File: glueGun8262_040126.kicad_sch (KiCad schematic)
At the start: 35 parts, among them CN1 KF243-5.0-2P, CN2 KF243-5.0-2P, CN3 KF243-5.0-2P, CN4 KF243-5.0-2P, CN5 KF243-5.0-2P, CN6 KF243-5.0-2P, U1 DRV8262DDWR, U2 DRV8262DDWR, U3 ESP32-S3-DEVKITC-1-N8R2, U4 INA4181A1IPWR

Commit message: ina240 schunts in series with sol
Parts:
- removed C11, C12, C13, C14: 10nf 100v, Capacitor_SMD:C_0603_1608Metric, symbol Device:C
- removed C15: 100nf 10v, Capacitor_SMD:C_0402_1005Metric, symbol Device:C
- removed R10, R7, R8, R9: 50mh, Resistor_SMD:R_1206_3216Metric, symbol Device:R
- removed U4: INA4181A1IPWR, easyeda2kicad:TSSOP-20_L6.5-W4.4-P0.65-LS6.4-BL, symbol easyeda2kicad:INA4181A1IPWR
- added C16: 10uf 50v, Capacitor_SMD:C_1206_3216Metric, symbol Device:C
- added C17: 22uf 10v, Capacitor_SMD:C_1206_3216Metric, symbol Device:C
- added C18, C19, C20, C21: 100nf, Capacitor_SMD:C_0603_1608Metric, symbol Device:C
- added CN7: KF243-5.0-2P, easyeda2kicad:CONN-TH_P5.00_KF243-5.0-2P, symbol easyeda2kicad:KF243-5.0-2P
- added CN9: KF243-5.0-4P, easyeda2kicad:CONN-TH_4P-P5.00_KF243-5.0-4P, symbol easyeda2kicad:KF243-5.0-4P
- added D1: D_Schottky, Package_TO_SOT_SMD:SOT-23, symbol Device:D_Schottky
- added D2, D3, D4, D5: green, LED_SMD:LED_0805_2012Metric, symbol Device:LED
- added NT1, NT3, NT4, NT5, NT6, NT7, NT8: NetTie_2, NetTie-2_SMD_Pad0.5mm, symbol Device:NetTie_2
- added NT2: NetTie_2, NetTie:NetTie-2_SMD_Pad0.5mm, symbol Device:NetTie_2
- added R11: 470r, Resistor_SMD:R_0201_0603Metric, symbol Device:R
- added R12, R13, R15, R16: 2.2k, Resistor_SMD:R_1206_3216Metric, symbol Device:R
- added R14: 5.1k, Resistor_SMD:R_0402_1005Metric, symbol Device:R
- added R17, R18, R19, R20: 40m, Resistor_SMD:R_2512_6332Metric, symbol Device:R
- added RN2: 10k, Resistor_SMD:R_Array_Convex_4x0603, symbol Device:R_Pack04
- added U10, U11, U6, U7: INA240A2DR, easyeda2kicad:SOIC-8_L4.9-W3.9-P1.27-LS6.0-BL, symbol easyeda2kicad:INA240A2DR
- added U5: 6N137, Package_DIP:DIP-8_W7.62mm, symbol Isolator:6N137
- added U8: K7805-1000R3_C2992391, easyeda2kicad:PWRM-TH_YLPTEC_K78XX-1000R3, symbol easyeda2kicad:K7805-1000R3_C2992391
- added U9: TLP281-4(GB-TP,J,F, easyeda2kicad:SOP-16_L10.3-W4.4-P1.27-LS7.0-BL, symbol easyeda2kicad:TLP281-4(GB-TP,J,F
- R1, R2, R3, R4, R5, R6: footprint Resistor_SMD:R_0805_2012Metric -> Resistor_SMD:R_0201_0603Metric
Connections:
- net U1_PGND12 is gone; now on net GND: U1.10 (PGND), U1.3 (PGND)
- net U1_PGND34 is gone; now on net GND: U1.13 (PGND), U1.20 (PGND)
- net U2_PGND12 is gone; now on net GND: U2.10 (PGND), U2.3 (PGND)
- net U2_PGND34 is gone; now on net GND: U2.13 (PGND), U2.20 (PGND)
- net +3V3: now also C18.1, C19.1, C20.1, C21.1, R14.1, RN2.5 (R4.2), RN2.6 (R3.2), RN2.7 (R2.2), RN2.8 (R1.2), U10.6 (VS), U11.6 (VS), U6.6 (VS), U7.6 (VS)
- net GND: now also CN6.2, C16.2, C17.2, C18.2, C19.2, C20.2, C21.2, U10.2 (GND), U10.3 (REF2), U10.7 (REF1), U11.2 (GND), U11.3 (REF2), U11.7 (REF1), U5.5 (GND), U6.2 (GND), U6.3 (REF2), U6.7 (REF1), U7.2 (GND), U7.3 (REF2), U7.7 (REF1), U8.2 (GND), U9.11 (EM), U9.13 (EM), U9.15 (EM), U9.2 (CAT), U9.4 (CAT), U9.6 (CAT), U9.8 (CAT), U9.9 (EM)
- net Gun1Vref: now also U6.5 (OUT)
- net Gun2Vref: now also U7.5 (OUT)
- net Gun3Vref: now also U10.5 (OUT)
- net Gun4Vref: now also U11.5 (OUT)
- net U2_OUT1: now reaches U2.4 (OUT1), U2.5 (OUT1), U2.6 (OUT1)
- net U2_OUT1: now also NT7.2, R19.2; no longer CN4.1
- net U2_OUT2: now reaches CN4.2, U2.7 (OUT2), U2.8 (OUT2), U2.9 (OUT2)
- net +5V: now reaches U3.J1_21 (5V0)
- net +5V: now also C17.1, U5.7 (EN), U5.8 (VCC), U8.3 (+VO)
- net Input_1_24v: now reaches U3.J3_10 (GPIO38)
- net Input_1_24v: now also RN2.1 (R1.1), U9.16 (COL)
- net Input_4_24v: now reaches U3.J3_16 (GPIO48)
- net Input_4_24v: now also RN2.4 (R4.1), U9.10 (COL)
- net Input_3_24v: now reaches U3.J3_17 (GPIO47)
- net Input_3_24v: now also RN2.3 (R3.1), U9.12 (COL)
- net Input_0_5v: now reaches U3.J3_18 (GPIO21)
- net Input_0_5v: now also R14.2, U5.6 (VO)
- net Input_2_24v: now reaches U3.J3_9 (MTCK/GPIO39)
- net Input_2_24v: now also RN2.2 (R2.1), U9.14 (COL)
- net U1_OUT3: now reaches U1.17 (OUT1), U1.18 (OUT1), U1.19 (OUT1)
- net U1_OUT3: now also NT4.2, R18.2; no longer CN3.1
- net U1_OUT4: now reaches U1.14 (OUT2), U1.15 (OUT2), U1.16 (OUT2)
- net U1_OUT4: now also CN3.1; no longer CN3.2
- net U1_OUT1: now reaches U1.4 (OUT1), U1.5 (OUT1), U1.6 (OUT1)
- net U1_OUT1: now also NT1.2, R17.2; no longer CN2.1
- net U1_OUT2: now reaches CN2.2, U1.7 (OUT2), U1.8 (OUT2), U1.9 (OUT2)
- net U2_OUT3: now reaches U2.17 (OUT1), U2.18 (OUT1), U2.19 (OUT1)
- net U2_OUT3: now also NT8.2, R20.2; no longer CN5.1
- net U2_OUT4: now reaches U2.14 (OUT2), U2.15 (OUT2), U2.16 (OUT2)
- net U2_OUT4: now also CN5.1; no longer CN5.2
- net at CN6.1: now also C16.1, U8.1 (VIN)
- new net: NT2.1, U6.1 (IN-)
- new net: CN2.1, NT2.2, R17.1
- new net: CN9.1, R12.1
- new net: D2.2 (A), R12.2
- new net: D3.1 (K), U9.3 (AN)
- new net: D3.2 (A), R13.2
- new net: NT3.1, U7.1 (IN-)
- new net: CN3.2, NT3.2, R18.1
- new net: CN9.4, R16.1
- new net: D5.2 (A), R16.2
- new net: D1.1 (K), R11.1
- new net: CN7.1, D1.2 (A)
- new net: CN4.1, NT5.2, R19.1
- new net: NT1.1, U6.8 (IN+)
- new net: D4.1 (K), U9.5 (AN)
- new net: D4.2 (A), R15.2
- new net: R11.2, U5.2 (A)
- new net: CN5.2, NT6.2, R20.1
- new net: NT6.1, U11.1 (IN-)
- new net: NT8.1, U11.8 (IN+)
- new net: NT7.1, U10.8 (IN+)
- new net: CN7.2, U5.3 (C)
- new net: CN9.2, R13.1
- new net: CN9.3, R15.1
- new net: NT5.1, U10.1 (IN-)
- new net: NT4.1, U7.8 (IN+)
- new net: D2.1 (K), U9.1 (AN)
- new net: D5.1 (K), U9.7 (AN)
- no-connect marks 8 -> 33
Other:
- note added: "5v input"
- note added: "Inputs"
- moved on the sheet: C1, C10, C2, C3, C4, C5, C6, C7, C8, C9, CN1, CN2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

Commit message: cont
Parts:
- removed NT1, NT3, NT4, NT5, NT6, NT7, NT8: NetTie_2, NetTie-2_SMD_Pad0.5mm, symbol Device:NetTie_2
- removed NT2: NetTie_2, NetTie:NetTie-2_SMD_Pad0.5mm, symbol Device:NetTie_2
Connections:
- net U1_OUT1: now also U6.8 (IN+)
- net U1_OUT3: now also U7.8 (IN+)
- net U2_OUT1: now also U10.8 (IN+)
- net U2_OUT3: now also U11.8 (IN+)
- net at U6.1 (IN-): now also CN2.1, R17.1
- net at U7.1 (IN-): now also CN3.2, R18.1
- net at CN4.1, R19.1: now also U10.1 (IN-)
- net at CN5.2, R20.1: now also U11.1 (IN-)

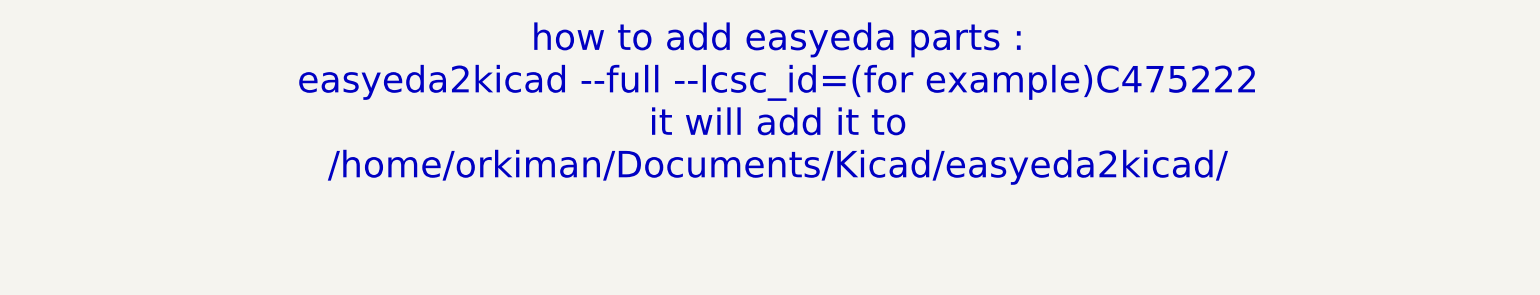
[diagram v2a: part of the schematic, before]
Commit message: cont arranging board. and easyeda models now in project folder
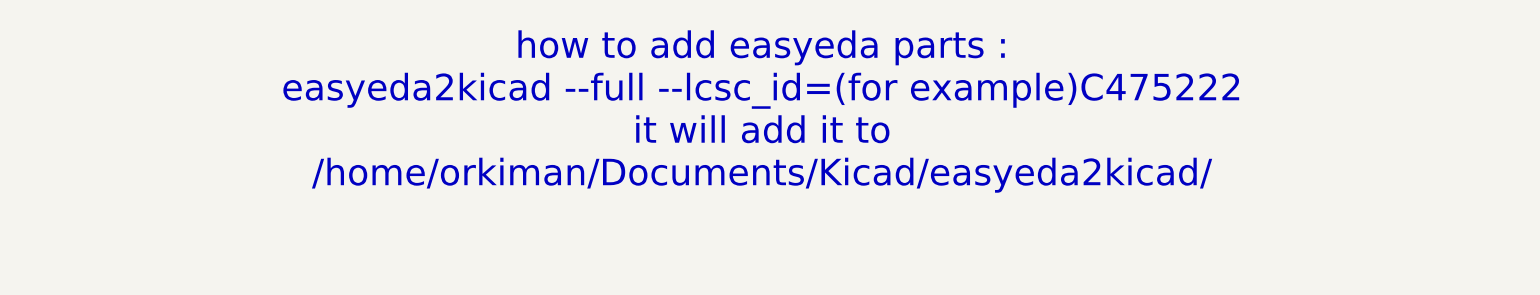
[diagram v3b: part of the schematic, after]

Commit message: cont rearrange pcb
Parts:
- C10, C6: footprint Capacitor_SMD:C_0402_1005Metric -> Capacitor_SMD:C_0603_1608Metric
- R1, R11, R2, R3, R4, R5, R6: footprint Resistor_SMD:R_0201_0603Metric -> Resistor_SMD:R_0603_1608Metric
- R14: footprint Resistor_SMD:R_0402_1005Metric -> Resistor_SMD:R_0603_1608Metric

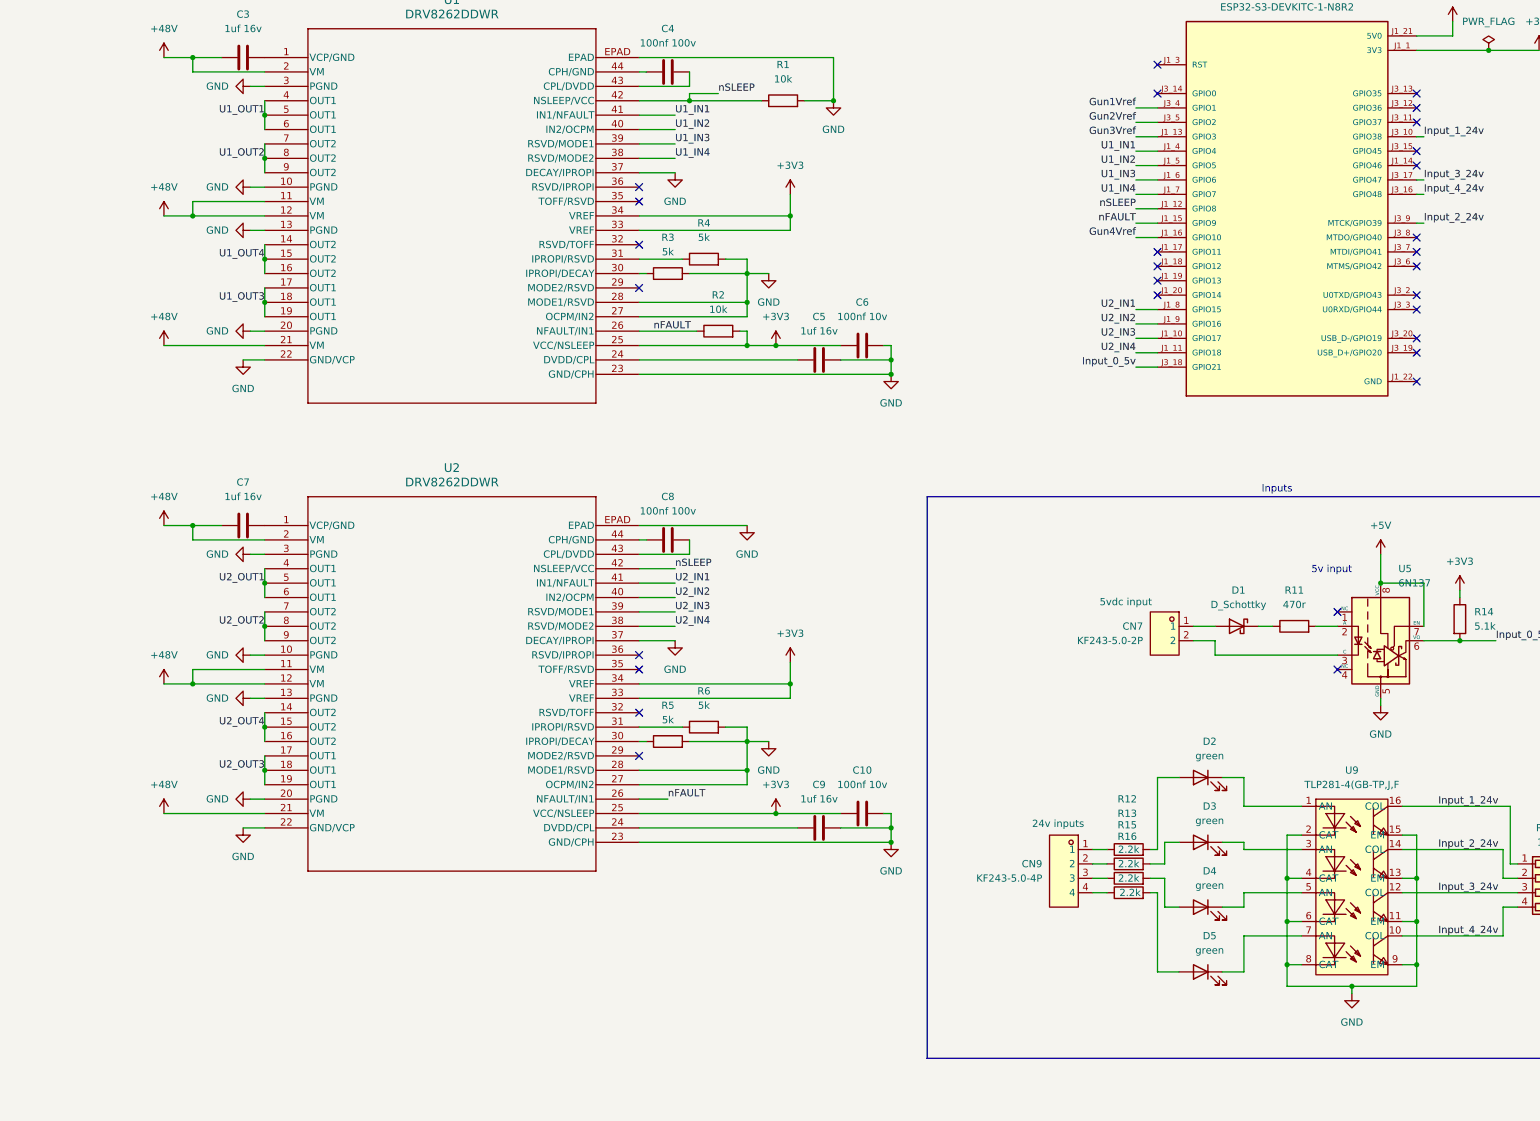
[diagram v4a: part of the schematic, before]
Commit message: high power routed and locked
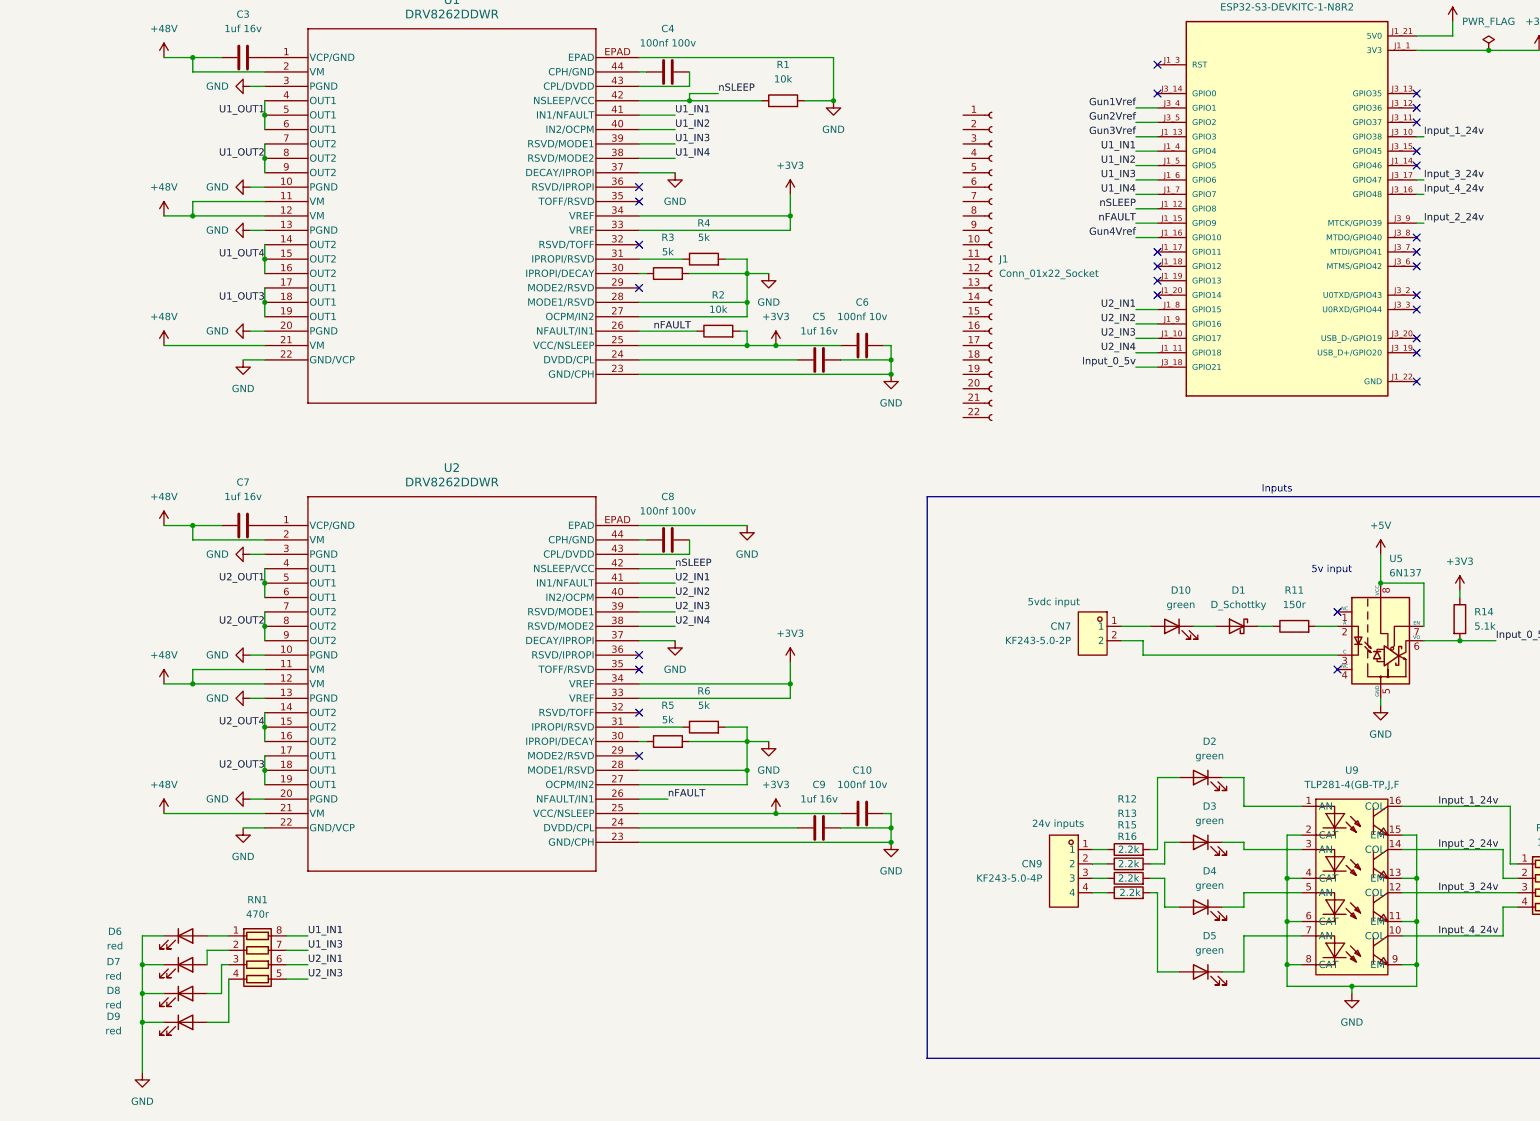
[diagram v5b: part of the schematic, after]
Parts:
- added D10: green, LED_SMD:LED_0805_2012Metric, symbol Device:LED
- added D6, D7, D8, D9: red, LED_SMD:LED_0805_2012Metric, symbol Device:LED
- added J1: Conn_01x22_Socket, symbol Connector:Conn_01x22_Socket
- added RN1: 470r, Resistor_SMD:R_Array_Convex_4x0603, symbol Device:R_Pack04
- R11: value 470r -> 150r
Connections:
- net GND: now also D6.1 (K), D7.1 (K), D8.1 (K), D9.1 (K)
- net U1_IN1: now also RN1.8 (R1.2)
- net U1_IN3: now also RN1.7 (R2.2)
- net U2_IN1: now also RN1.6 (R3.2)
- net U2_IN3: now also RN1.5 (R4.2)
- net at D1.2 (A): now also D10.1 (K); no longer CN7.1
- new net: D6.2 (A), RN1.1 (R1.1)
- new net: D8.2 (A), RN1.3 (R3.1)
- new net: D7.2 (A), RN1.2 (R2.1)
- new net: D9.2 (A), RN1.4 (R4.1)
- new net: CN7.1, D10.2 (A)
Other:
- moved on the sheet: CN7
